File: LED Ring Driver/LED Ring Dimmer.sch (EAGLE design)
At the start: 65 parts, among them IC1 TPS54202DDCR, IC2 LD1117S33TR, M1 M_HOLE_3M, M2 M_HOLE_3M, M3 M_HOLE_3M, M4 M_HOLE_3M, Q1 2N7002, U1 TPS92515QDGQTQ1DGQ0010A_M, X1 WF2549-2WS05S0B01, X2 X01_PAD-2MM, X3 X01_PAD-2MM, X4 X01_PAD-2MM, X5 X01_PAD-2MM, X6 X01_PAD-2MM

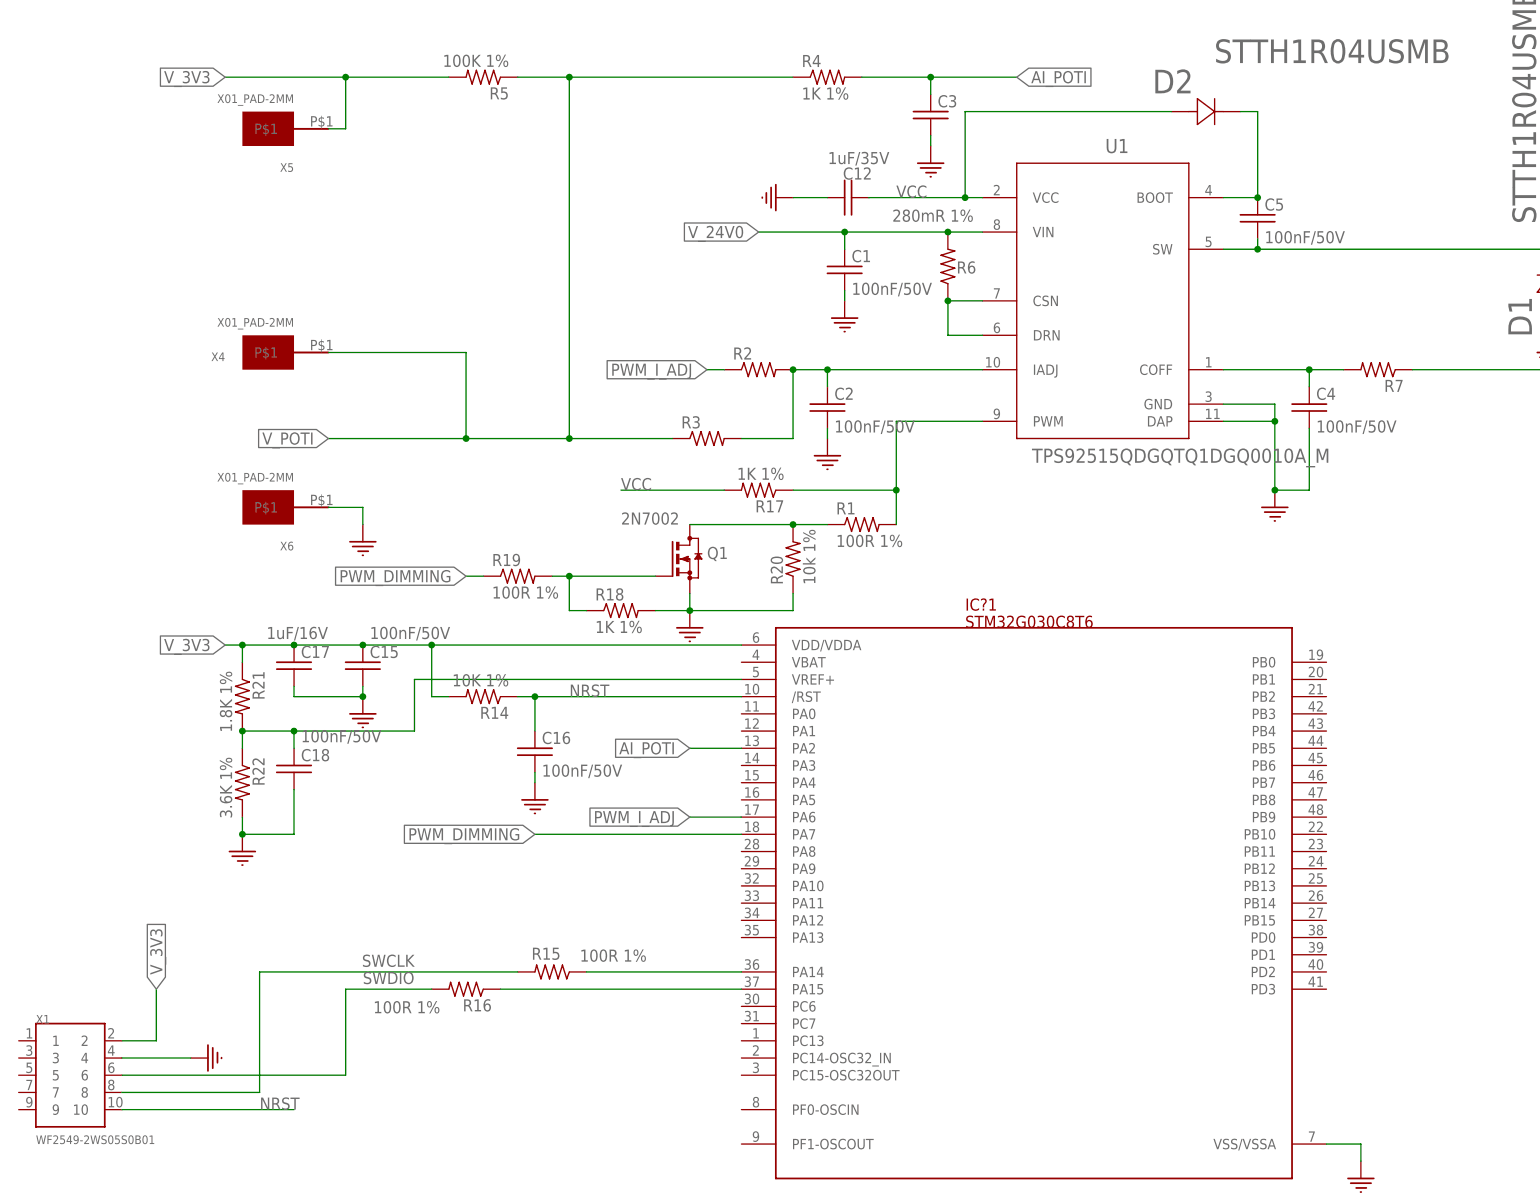
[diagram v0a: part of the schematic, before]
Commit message: HW modification Schematic + Layout
SWDIO was connected to wrong pin, now modified
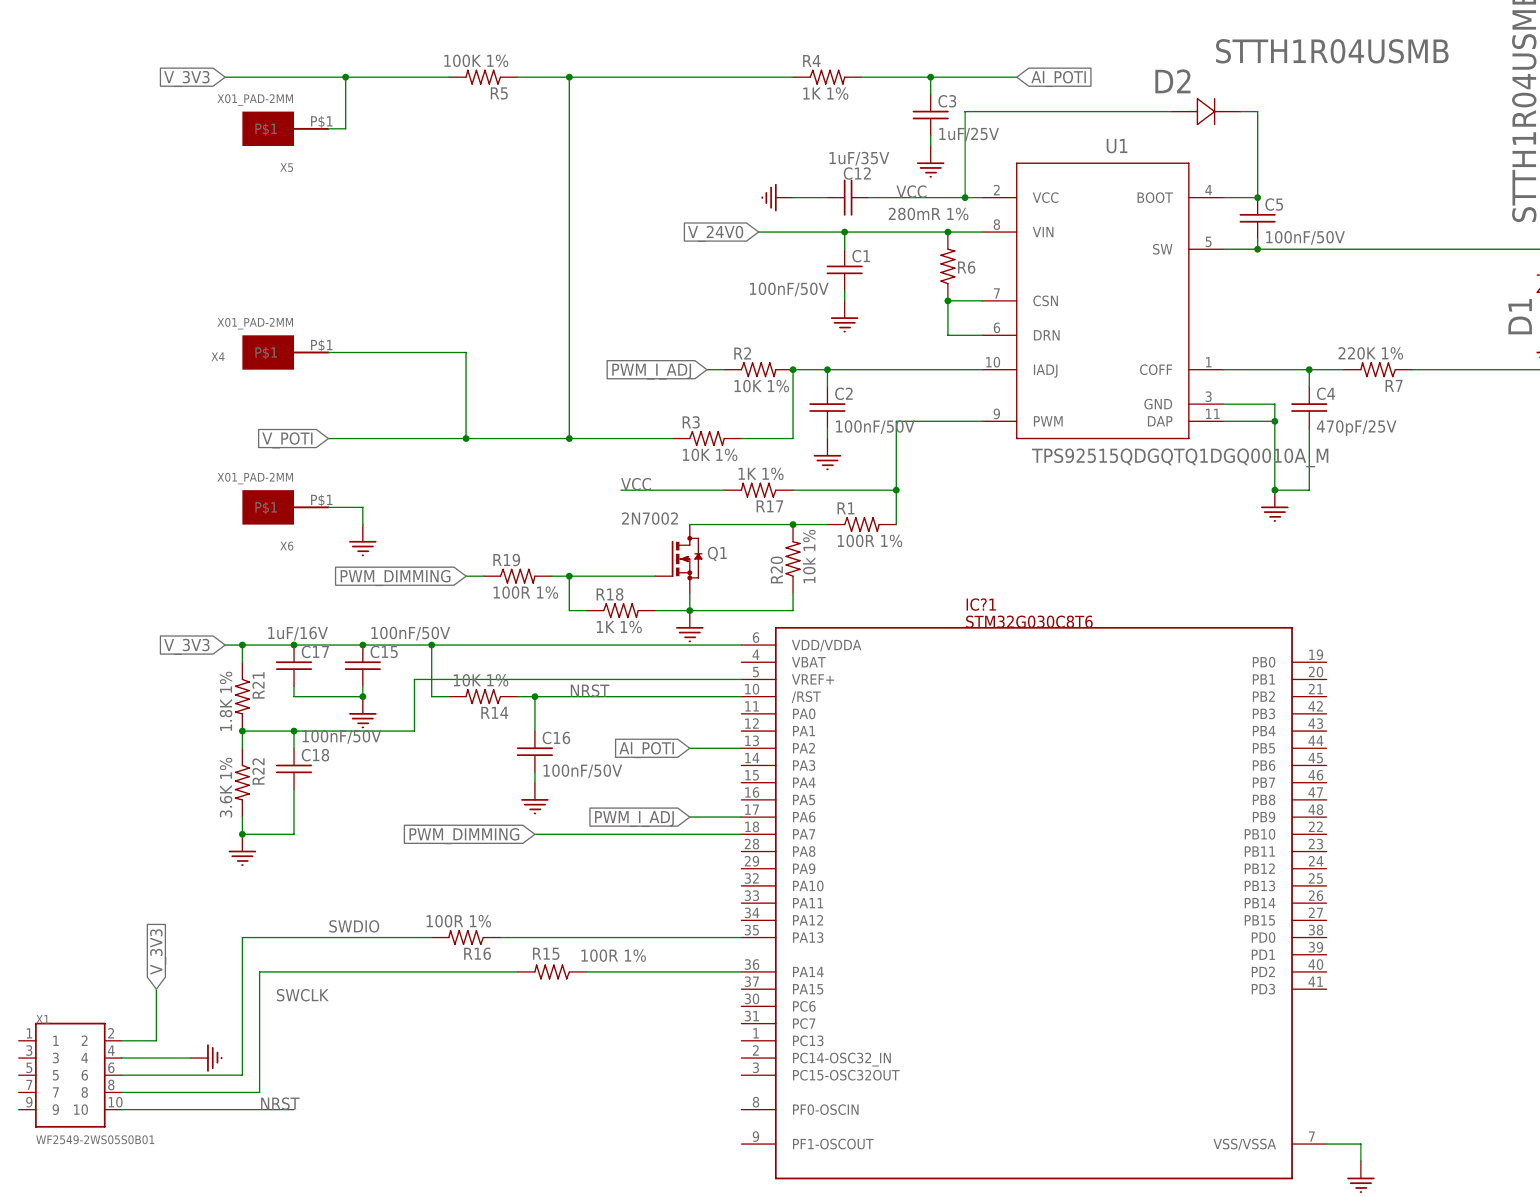
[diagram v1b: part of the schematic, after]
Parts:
- C3: value (none) -> 1uF/25V
- C4: value 100nF/50V -> 470pF/25V
- R2, R3: value (none) -> 10K 1%
- R7: value (none) -> 220K 1%
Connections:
- removed net N$19: IC?1.PA15, R16.1
- new net N$17: IC?1.PA13, R16.1
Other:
- moved on the sheet: R16
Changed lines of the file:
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@@
 <setting verticaltext="up"/>
 </settings>
-<grid distance="0.1" unitdist="inch" unit="inch" style="lines" multiple="1" display="yes" altdistance="0.01" altunitdist="inch" altunit="inch"/>
+<grid distance="0.1" unitdist="inch" unit="inch" style="lines" multiple="1" display="no" altdistance="0.01" altunitdist="inch" altunit="inch"/>
 <layers>
 <layer number="1" name="Top" color="4" fill="1" visible="no" active="no"/>
@@
 <part name="GND2" library="Labops_Lib_AH" deviceset="GND" device=""/>
 <part name="R1" library="Labops_Lib_AH" deviceset="R_0603" device="" value="100R 1%"/>
-<part name="R2" library="Labops_Lib_AH" deviceset="R_0603" device=""/>
+<part name="R2" library="Labops_Lib_AH" deviceset="R_0603" device="" value="10K 1%"/>
 <part name="C2" library="Labops_Lib_AH" deviceset="C_0603" device="EIA0603" value="100nF/50V"/>
-<part name="R3" library="Labops_Lib_AH" deviceset="R_0603" device=""/>
+<part name="R3" library="Labops_Lib_AH" deviceset="R_0603" device="" value="10K 1%"/>
 <part name="GND3" library="Labops_Lib_AH" deviceset="GND" device=""/>
-<part name="C3" library="Labops_Lib_AH" deviceset="C_0603" device="EIA0603"/>
+<part name="C3" library="Labops_Lib_AH" deviceset="C_0603" device="EIA0603" value="1uF/25V"/>
 <part name="GND4" library="Labops_Lib_AH" deviceset="GND" device=""/>
 <part name="R4" library="Labops_Lib_AH" deviceset="R_0603" device="" value="1K 1%"/>
 <part name="R5" library="Labops_Lib_AH" deviceset="R_0603" device="" value="100K 1%"/>
-<part name="C4" library="Labops_Lib_AH" deviceset="C_0603" device="EIA0603" value="100nF/50V"/>
+<part name="C4" library="Labops_Lib_AH" deviceset="C_0603" device="EIA0603" value="470pF/25V"/>
 <part name="R6" library="Labops_Lib_AH" deviceset="R_1206" device="EIA1206" value="280mR 1%"/>
-<part name="R7" library="Labops_Lib_AH" deviceset="R_0603" device=""/>
+<part name="R7" library="Labops_Lib_AH" deviceset="R_0603" device="" value="220K 1%"/>
 <part name="C5" library="Labops_Lib_AH" deviceset="C_0603" device="EIA0603" value="100nF/50V"/>
 <part name="D1" library="Labops_Lib_AH" deviceset="STTH1R04U" device="SMB"/>
@@
 <instance part="C1" gate="G$1" x="160.02" y="139.7" smashed="yes">
 <attribute name="NAME" x="161.036" y="140.335" size="1.778" layer="95"/>
-<attribute name="VALUE" x="161.036" y="135.509" size="1.778" layer="96"/>
+<attribute name="VALUE" x="145.796" y="135.509" size="1.778" layer="96"/>
 </instance>
 <instance part="GND1" gate="1" x="160.02" y="132.08" smashed="yes"/>
@@
 <instance part="R6" gate="G$1" x="175.26" y="139.7" smashed="yes" rot="R90">
 <attribute name="NAME" x="176.53" y="138.6586" size="1.778" layer="95"/>
-<attribute name="VALUE" x="179.07" y="148.082" size="1.778" layer="96" rot="R180"/>
+<attribute name="VALUE" x="166.37" y="146.558" size="1.778" layer="96"/>
 </instance>
 <instance part="R7" gate="G$1" x="238.76" y="124.46" smashed="yes" rot="R180">
@@
 <attribute name="VALUE" x="130.81" y="38.862" size="1.778" layer="96" rot="R180"/>
 </instance>
-<instance part="R16" gate="G$1" x="104.14" y="33.02" smashed="yes" rot="R180">
-<attribute name="NAME" x="107.95" y="31.5214" size="1.778" layer="95" rot="R180"/>
-<attribute name="VALUE" x="100.33" y="31.242" size="1.778" layer="96" rot="R180"/>
+<instance part="R16" gate="G$1" x="104.14" y="40.64" smashed="yes" rot="R180">
+<attribute name="NAME" x="107.95" y="39.1414" size="1.778" layer="95" rot="R180"/>
+<attribute name="VALUE" x="107.95" y="43.942" size="1.778" layer="96" rot="R180"/>
 </instance>
 <instance part="X1" gate="G$1" x="43.18" y="20.32" smashed="yes">
@@
 </segment>
 </net>
-<net name="N$19" class="0">
-<segment>
-<pinref part="R16" gate="G$1" pin="1"/>
-<pinref part="IC?1" gate="G$1" pin="PA15"/>
-<wire x1="109.22" y1="33.02" x2="144.78" y2="33.02" width="0.1524" layer="91"/>
-</segment>
-</net>
 <net name="SWDIO" class="0">
 <segment>
 <pinref part="R16" gate="G$1" pin="2"/>
-<wire x1="99.06" y1="33.02" x2="86.36" y2="33.02" width="0.1524" layer="91"/>
-<label x="96.52" y="35.56" size="1.778" layer="95" rot="R180"/>
+<wire x1="99.06" y1="40.64" x2="71.12" y2="40.64" width="0.1524" layer="91"/>
+<label x="91.44" y="43.18" size="1.778" layer="95" rot="R180"/>
 <pinref part="X1" gate="G$1" pin="6"/>
-<wire x1="86.36" y1="33.02" x2="86.36" y2="20.32" width="0.1524" layer="91"/>
-<wire x1="86.36" y1="20.32" x2="53.34" y2="20.32" width="0.1524" layer="91"/>
+<wire x1="71.12" y1="40.64" x2="71.12" y2="20.32" width="0.1524" layer="91"/>
+<wire x1="71.12" y1="20.32" x2="53.34" y2="20.32" width="0.1524" layer="91"/>
 </segment>
 </net>
@@
 <pinref part="R15" gate="G$1" pin="2"/>
 <wire x1="111.76" y1="35.56" x2="73.66" y2="35.56" width="0.1524" layer="91"/>
-<label x="96.52" y="38.1" size="1.778" layer="95" rot="R180"/>
+<label x="83.82" y="33.02" size="1.778" layer="95" rot="R180"/>
 <pinref part="X1" gate="G$1" pin="8"/>
 <wire x1="73.66" y1="35.56" x2="73.66" y2="17.78" width="0.1524" layer="91"/>
@@
 </segment>
 </net>
+<net name="N$17" class="0">
+<segment>
+<pinref part="R16" gate="G$1" pin="1"/>
+<pinref part="IC?1" gate="G$1" pin="PA13"/>
+<wire x1="109.22" y1="40.64" x2="144.78" y2="40.64" width="0.1524" layer="91"/>
+</segment>
+</net>
